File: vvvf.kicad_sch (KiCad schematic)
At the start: 45 parts, among them Q1 Q_NIGBT_GCE, Q2 Q_NIGBT_GCE, Q3 IPDD60R037CM8XTMA1, Q4 IPDD60R037CM8XTMA1, Q5 IPDD60R037CM8XTMA1, SW1 SW_Push, U1 TLP152, U2 TLP152, U3 UCC21520ADW, U4 TLP152, U5 ACS772ECB-400B-PFF-T

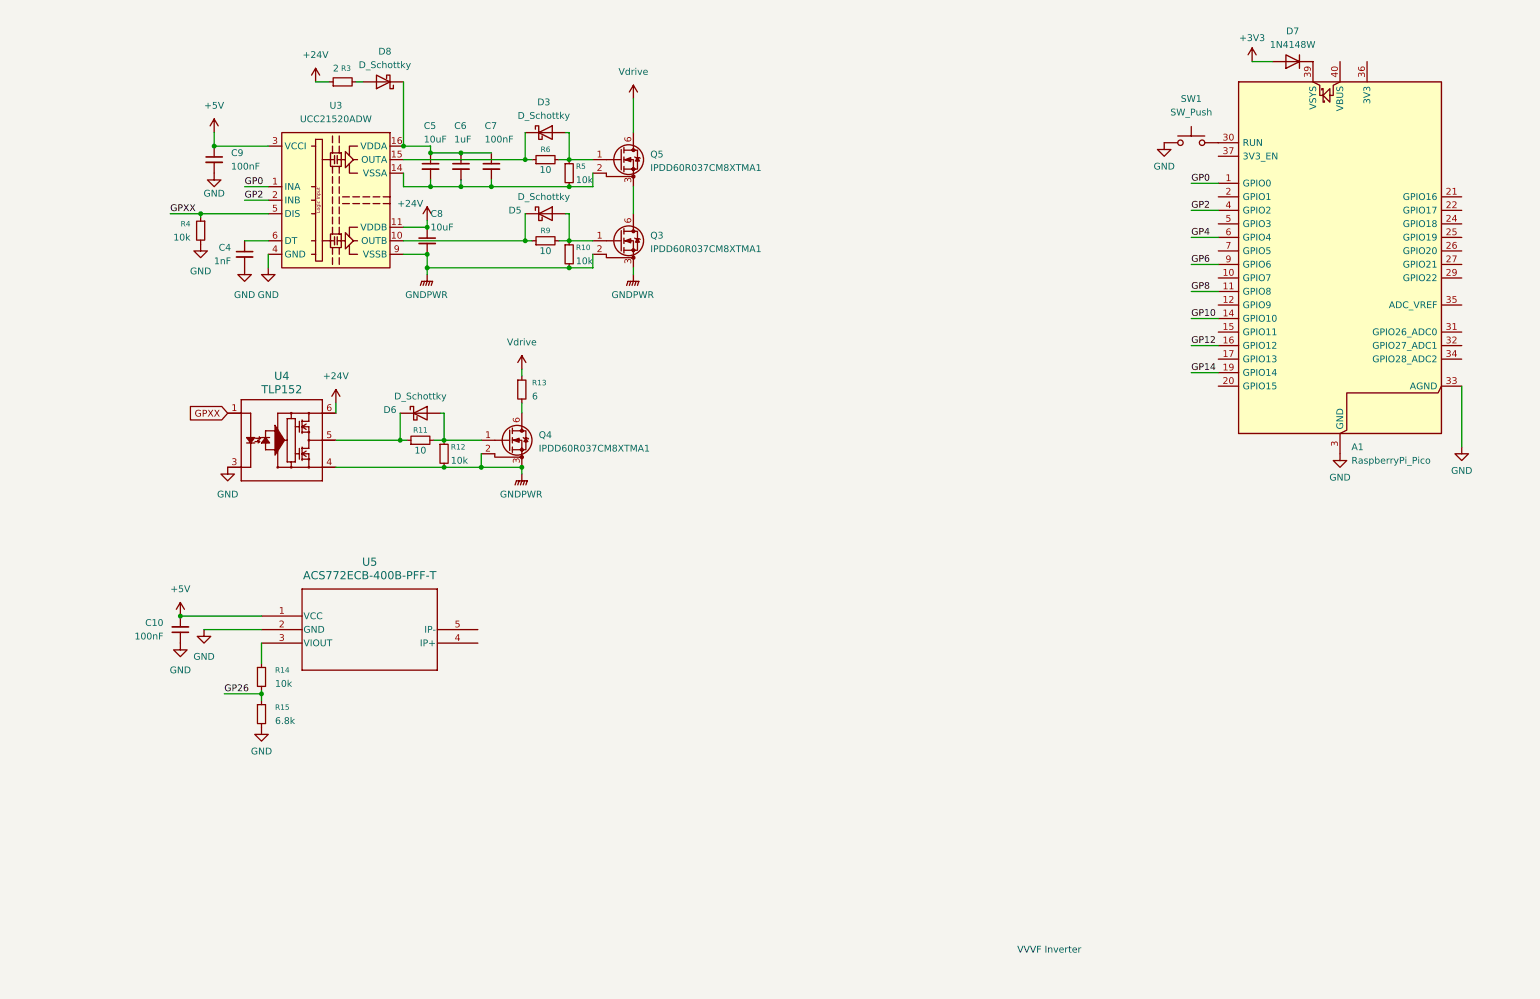
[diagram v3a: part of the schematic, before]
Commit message: Clean up schematic
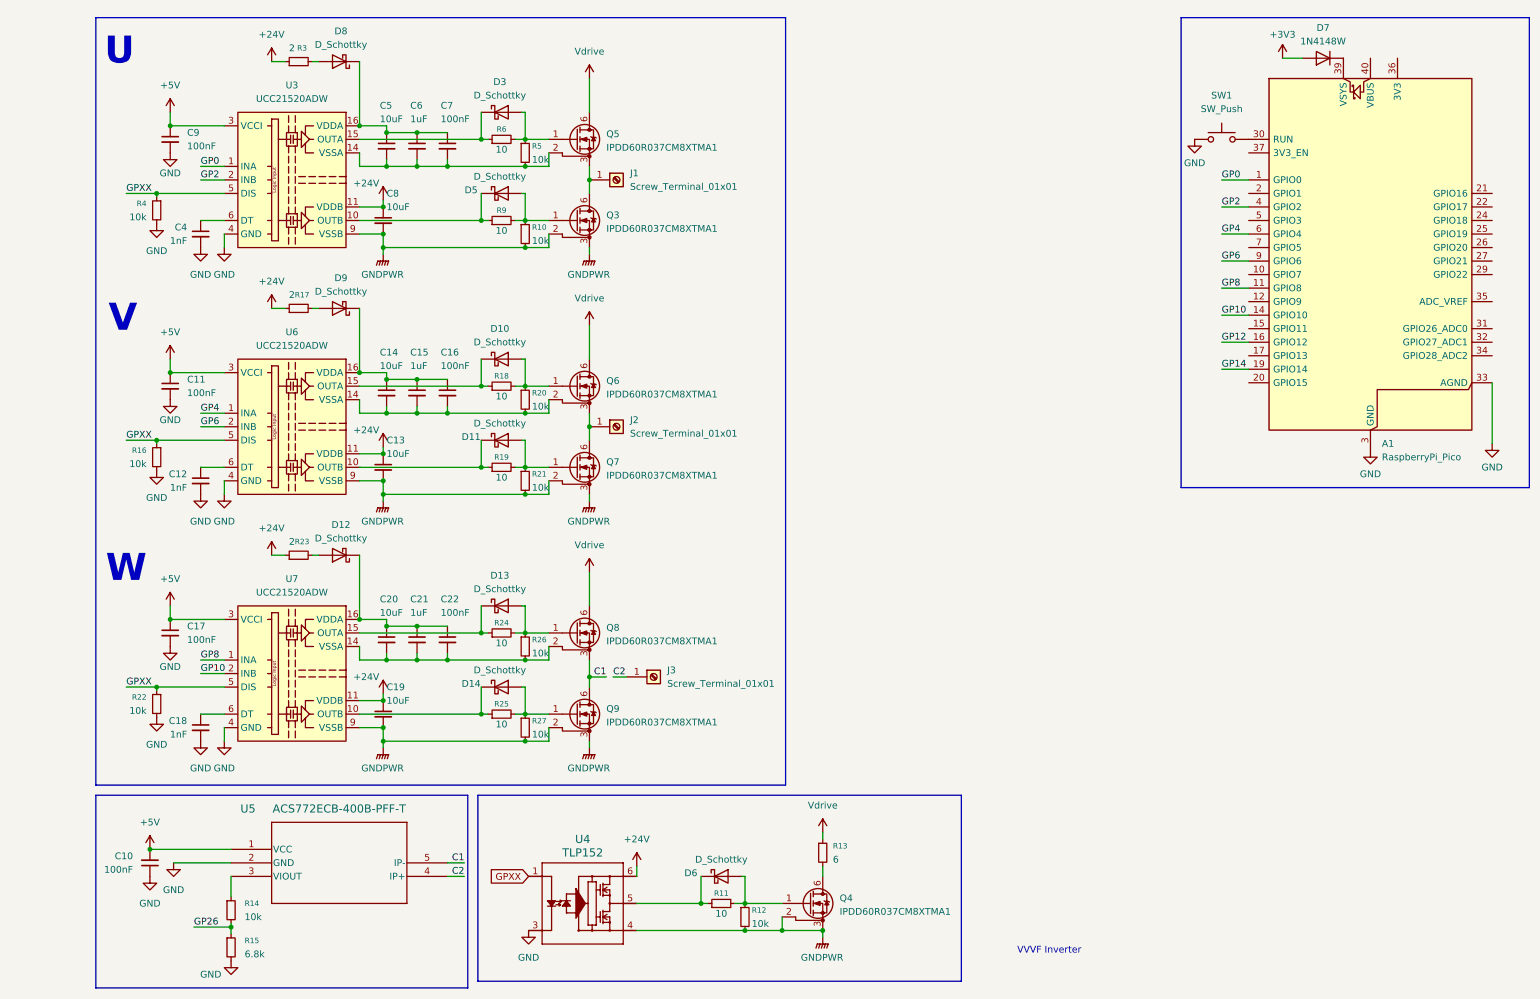
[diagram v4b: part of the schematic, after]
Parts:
- added C11, C16, C17, C22: 100nF, symbol Device:C_Small
- added C12, C18: 1nF, symbol Device:C_Small
- added C13, C14, C19, C20: 10uF, symbol Device:C_Small
- added C15, C21: 1uF, symbol Device:C_Small
- added D10, D11, D12, D13, D14, D9: D_Schottky, symbol Device:D_Schottky
- added J1, J2, J3: Screw_Terminal_01x01, symbol Connector:Screw_Terminal_01x01
- added Q6, Q7, Q8, Q9: IPDD60R037CM8XTMA1, Package_TO_SOT_SMD:Infineon_PG-HDSOP-10-1, symbol Transistor_FET:IPDD60R050G7
- added R16, R20, R21, R22, R26, R27: 10k, symbol Device:R_Small
- added R17, R23: 2, symbol Device:R_Small
- added R18, R19, R24, R25: 10, symbol Device:R_Small
- added U6, U7: UCC21520ADW, Package_SO:SOIC-16W_7.5x10.3mm_P1.27mm, symbol Driver_FET:UCC21520ADW
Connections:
- net +24V: now also C13.1, C19.1, R17.1, R23.1, U6.11 (VDDB), U7.11 (VDDB)
- net +5V: now also C11.1, C17.1, U6.3 (VCCI), U6.8 (VCCI), U7.3 (VCCI), U7.8 (VCCI)
- net GND: now also C11.2, C12.2, C17.2, C18.2, R16.2, R22.2, U6.4 (GND), U7.4 (GND)
- net GNDPWR: now also C13.2, C19.2, Q7.2 (DS), Q7.3 (PS), Q7.4 (PS), Q7.5 (PS), Q9.2 (DS), Q9.3 (PS), Q9.4 (PS), Q9.5 (PS), R21.2, R27.2, U6.9 (VSSB), U7.9 (VSSB)
- net GP10: now also U7.2 (INB)
- net GP4: now also U6.1 (INA)
- net GP6: now also U6.2 (INB)
- net GP8: now also U7.1 (INA)
- net GPXX: now also R16.1, R22.1, U6.5 (DIS), U7.5 (DIS)
- net Vdrive: now also Q6.10 (D), Q6.6 (D), Q6.7 (D), Q6.8 (D), Q6.9 (D), Q8.10 (D), Q8.6 (D), Q8.7 (D), Q8.8 (D), Q8.9 (D)
- net C2: now reaches U5.4 (IP+)
- net C2: now also J3.1 (Pin_1)
- net C1: now reaches U5.5 (IP-)
- net C1: now also Q8.3 (PS), Q8.4 (PS), Q8.5 (PS), Q9.10 (D), Q9.6 (D), Q9.7 (D), Q9.8 (D), Q9.9 (D)
- net at Q3.10 (D), Q3.6 (D), Q3.7 (D)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: now also J1.1 (Pin_1)
- new net: J2.1 (Pin_1), Q6.3 (PS), Q6.4 (PS), Q6.5 (PS), Q7.10 (D), Q7.6 (D), Q7.7 (D), Q7.8 (D), Q7.9 (D)
- new net: D13.1 (K), R24.1, U7.15 (OUTA)
- new net: D13.2 (A), Q8.1 (G), R24.2, R26.1
- new net: D10.1 (K), R18.1, U6.15 (OUTA)
- new net: D10.2 (A), Q6.1 (G), R18.2, R20.1
- new net: C20.1, C21.1, C22.1, D12.1 (K), U7.16 (VDDA)
- new net: D12.2 (A), R23.2
- new net: D11.1 (K), R19.1, U6.10 (OUTB)
- new net: C14.2, C15.2, C16.2, Q6.2 (DS), R20.2, U6.14 (VSSA)
- new net: C14.1, C15.1, C16.1, D9.1 (K), U6.16 (VDDA)
- new net: C12.1, U6.6 (DT)
- new net: D9.2 (A), R17.2
- new net: C18.1, U7.6 (DT)
- new net: C20.2, C21.2, C22.2, Q8.2 (DS), R26.2, U7.14 (VSSA)
- new net: D14.2 (A), Q9.1 (G), R25.2, R27.1
- new net: D11.2 (A), Q7.1 (G), R19.2, R21.1
- new net: D14.1 (K), R25.1, U7.10 (OUTB)
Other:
- note added: "U"
- note added: "V"
- note added: "W"
- moved on the sheet: A1, C10, C4, C5, C6, C7, C8, C9, D3, D5, D6, D7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

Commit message: Push changes at the end of the day
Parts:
- removed D10, D11, D12, D13, D14, D3, D5, D8, D9: D_Schottky, symbol Device:D_Schottky
- added D10, D11, D12, D13, D15, D3, D5, D8, D9: SUF4007, Diode_SMD:D_MELF_Handsoldering, symbol Device:D
- C10, C11, C12, C13, C14, C15, C16, C17, C18, C19, C20, C21, C22, C4, C5, C6, C7, C8, C9: footprint (none) -> Capacitor_SMD:C_0603_1608Metric_Pad1.08x0.95mm_HandSolder
- R10, R11, R12, R14, R16, R17, R18, R19, R20, R21, R22, R23, R24, R25, R26, R27, R3, R4, R5, R6, R9: footprint (none) -> Resistor_SMD:R_0603_1608Metric_Pad0.98x0.95mm_HandSolder
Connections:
- net at R24.1, U7.15 (OUTA): now also D11.1 (K)
- net at Q8.1 (G), R24.2, R26.1: now also D11.2 (A)
- net at R18.1, U6.15 (OUTA): now also D10.1 (K)
- net at Q6.1 (G), R18.2, R20.1: now also D10.2 (A)
- net at Q3.1 (G), R10.1, R9.2: now also D3.2 (A)
- net at C20.1, C21.1, C22.1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: now also D12.1 (K)
- net at R23.2: now also D12.2 (A)
- net at Q5.1 (G), R5.1, R6.2: now also D8.2 (A)
- net at C5.1, C6.1, C7.1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: now also D15.1 (K)
- net at R19.1, U6.10 (OUTB): now also D5.1 (K)
- net at C14.1, C15.1, C16.1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: now also D9.1 (K)
- net at R17.2: now also D9.2 (A)
- net at R6.1, U3.15 (OUTA): now also D8.1 (K)
- net at Q9.1 (G), R25.2, R27.1: now also D13.2 (A)
- net at R9.1, U3.10 (OUTB): now also D3.1 (K)
- net at R3.2: now also D15.2 (A)
- net GP7: now reaches A1.10 (GPIO7)
- net GP9: now reaches A1.12 (GPIO9)
- net GP11: now reaches A1.15 (GPIO11)
- net GP13: now reaches A1.17 (GPIO13)
- net GP1: now reaches A1.2 (GPIO1)
- net GP15: now reaches A1.20 (GPIO15)
- net GP16: now reaches A1.21 (GPIO16)
- net GP17: now reaches A1.22 (GPIO17)
- net GP18: now reaches A1.24 (GPIO18)
- net GP19: now reaches A1.25 (GPIO19)
- net GP20: now reaches A1.26 (GPIO20)
- net GP21: now reaches A1.27 (GPIO21)
- net GP21: now also A1.29 (GPIO22)
- net ADC0: now reaches A1.31 (GPIO26_ADC0)
- net ADC1: now reaches A1.32 (GPIO27_ADC1)
- net ADC2: now reaches A1.34 (GPIO28_ADC2)
- net GP3: now reaches A1.5 (GPIO3)
- net GP5: now reaches A1.7 (GPIO5)
- net at Q7.1 (G), R19.2, R21.1: now also D5.2 (A)
- net at R25.1, U7.10 (OUTB): now also D13.1 (K)
- no-connect marks 0 -> 3
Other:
- moved on the sheet: A1, C10, D7, R14, R15, SW1, U5

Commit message: Started with basic layout
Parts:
- removed D6: D_Schottky, symbol Device:D_Schottky
- removed U5: ACS772ECB-400B-PFF-T, Snapeda:ACS772_PFF_ALM, symbol Snapeda:ACS772ECB-400B-PFF-T
- added C23, C25, C27, C29, C31, C33: 1uF, Snapeda:B32923C3105M000_CAPRR2250W80L2650T1100H2050, symbol Device:C_Small
- added C24, C26, C28, C30, C32, C34: 100nF, Snapeda:B32922C3104K289_CAPRR1500W80L1800T500H1050, symbol Device:C_Small
- added D6: ES1D, Diode_SMD:D_SMA_Handsoldering, symbol Device:D
- added J4, J5: Screw_Terminal_01x01, symbol Connector:Screw_Terminal_01x01
- added J6: Screw_Terminal_01x02, symbol Connector:Screw_Terminal_01x02
- added U5: ACS770xCB-200B-PFF, Sensor_Current:Allegro_CB_PFF, symbol Sensor_Current:ACS770xCB-200B-PFF
- D10, D11, D12, D13, D15, D3, D5, D8, D9: value SUF4007 -> ES1D; footprint Diode_SMD:D_MELF_Handsoldering -> Diode_SMD:D_SMA_Handsoldering; Digikey Part 4878-SUF4007CT-ND -> ES1DFSTR-ND
- R10, R12, R16, R20, R21, R22, R26, R27, R4, R5: value 10k -> 4.7k
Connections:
- net +5V: now also U5.1 (VCC)
- net C1: now also C20.2, C21.2, C22.2, Q8.2 (DS), R26.2, U7.14 (VSSA), C31.2, C32.2, C33.1, C34.1, U5.4 (IP+)
- net C2: now also U5.5 (IP-)
- net GND: now also U5.2 (GND)
- net GNDPWR: now also C25.2, C26.2, C29.2, C30.2, C33.2, C34.2
- net GP13: now also R4.1, U3.5 (DIS)
- net GP14: now also R16.1, U6.5 (DIS)
- net GP15: now also R22.1, U7.5 (DIS)
- net GPXX: no longer R16.1, R22.1, R4.1, U3.5 (DIS), U6.5 (DIS), U7.5 (DIS)
- net Vdrive: now also C23.1, C24.1, C27.1, C28.1, C31.1, C32.1
- net at J2.1 (Pin_1), Q6.3 (PS), Q6.4 (PS)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: now also C14.2, C15.2, C16.2, Q6.2 (DS), R20.2, U6.14 (VSSA), C27.2, C28.2, C29.1, C30.1
- net at R14.1: now also U5.3 (VIOUT)
- net at Q4.1 (G), R11.2, R12.1: now also D6.2 (A)
- net at C5.2, C6.2, C7.2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: now also J1.1 (Pin_1), Q3.10 (D), Q3.6 (D), Q3.7 (D), Q3.8 (D), Q3.9 (D), Q5.3 (PS), Q5.4 (PS), Q5.5 (PS), C23.2, C24.2, C25.1, C26.1
- net at R11.1, U4.5: now also D6.1 (K)
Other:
- moved on the sheet: C10, Q4, R11, R12, R13, R14, R15, U4

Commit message: Continue on layout
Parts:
- added C35: 10uF, symbol Device:C_Small
- added C36: 470pF, symbol Device:C_Small
- added PS1: ROE-1205S, Snapeda:ROE-1205S_CONV_ROE-1205S, symbol Snapeda:ROE-1205S
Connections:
- net +24V: no longer C13.1, C19.1, C8.1, R17.1, R23.1, R3.1, U3.11 (VDDB), U4.6, U6.11 (VDDB), U7.11 (VDDB)
- net +3V3: now also A1.36 (3V3); no longer D7.2 (A)
- net +5V: now also D7.2 (A), C36.2, PS1.4 (+VOUT)
- net GND: now also PS1.3 (-VOUT)
- net GNDPWR: now also J5.1 (Pin_1), J6.2 (Pin_2), C35.2, PS1.1 (-VIN)
- net Vdrive: now also J4.1 (Pin_1)
- net +12V: now reaches J6.1 (Pin_1)
- net +12V: now also C13.1, C19.1, C8.1, R17.1, R23.1, R3.1, U3.11 (VDDB), U4.6, U6.11 (VDDB), U7.11 (VDDB), C35.1, C36.1, PS1.2 (+VIN)
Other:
- moved on the sheet: J4, J5, J6

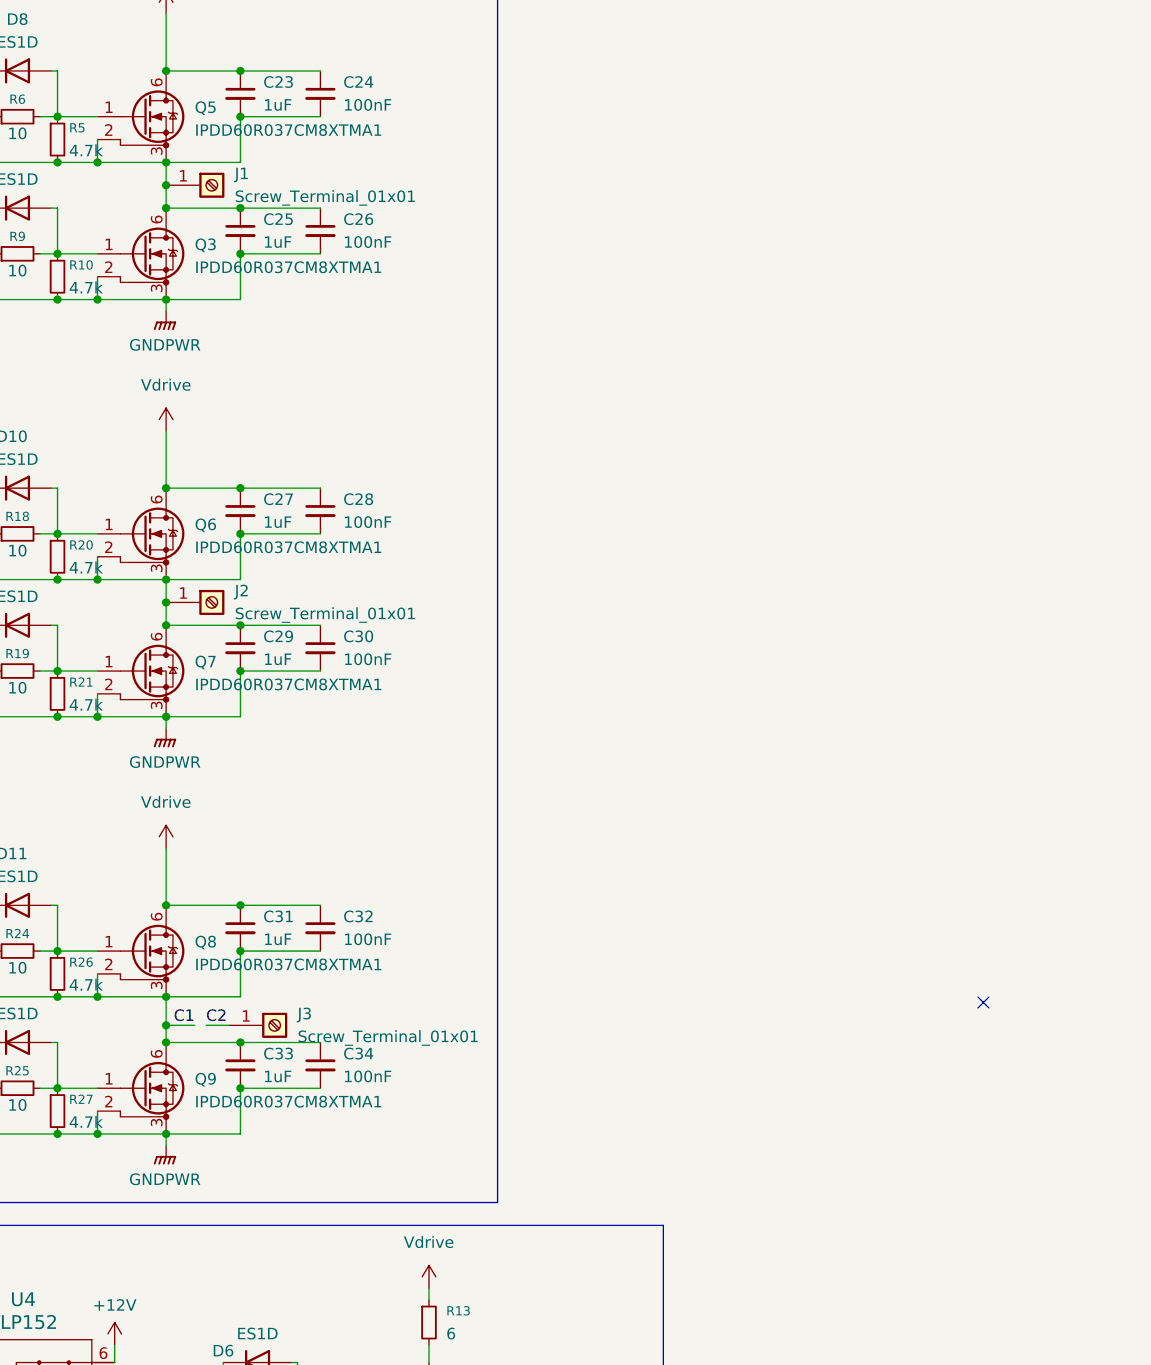
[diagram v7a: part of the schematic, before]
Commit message: Checkpoint before switching to an external IGBT array
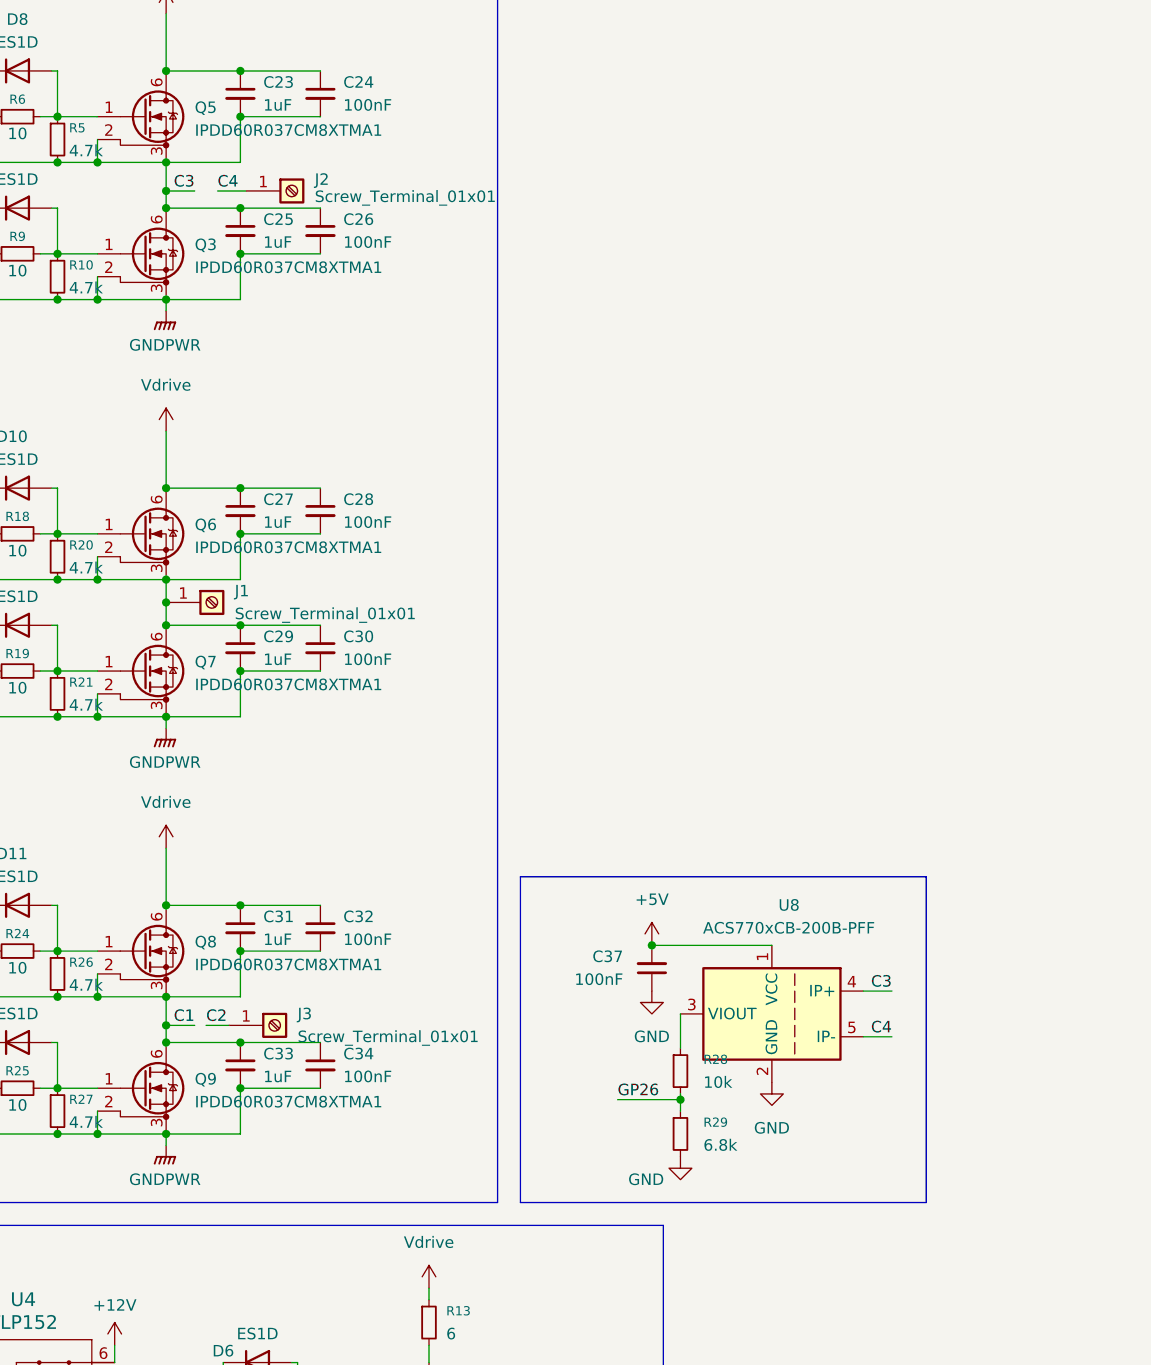
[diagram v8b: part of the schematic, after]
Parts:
- added C37: 100nF, Capacitor_SMD:C_0603_1608Metric_Pad1.08x0.95mm_HandSolder, symbol Device:C_Small
- added R28: 10k, Resistor_SMD:R_0603_1608Metric_Pad0.98x0.95mm_HandSolder, symbol Device:R_Small
- added R29: 6.8k, symbol Device:R_Small
- added U8: ACS770xCB-200B-PFF, Sensor_Current:Allegro_CB_PFF, symbol Sensor_Current:ACS770xCB-200B-PFF
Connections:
- net +5V: now also C37.2, U8.1 (VCC)
- net GND: now also C37.1, R29.2, U8.2 (GND)
- net GP26: now also R28.2, R29.1
- net at C14.2, C15.2, C16.2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: now also J1.1 (Pin_1); no longer J2.1 (Pin_1)
- net C3: now reaches C23.2, C24.2, C25.1, C26.1, C5.2, C6.2, C7.2, Q3.10 (D), Q3.6 (D), Q3.7 (D), Q3.8 (D), Q3.9 (D), Q5.2 (DS), Q5.3 (PS), Q5.4 (PS), Q5.5 (PS), R5.2, U3.14 (VSSA)
- net C3: now also U8.4 (IP+); no longer J1.1 (Pin_1)
- new net: R28.1, U8.3 (VIOUT)
- new net C4: J2.1 (Pin_1), U8.5 (IP-)
- no-connect marks 3 -> 2
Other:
- moved on the sheet: J1, J2
